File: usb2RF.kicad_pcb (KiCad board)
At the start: 4 copper layers, 40 x 15 mm, 38 parts, among them J1 USB_B_Micro, J2 SMA, J3 ARM 10Pin, U1 nRF24L01P, U2 XC6206P332MR, U3 USBLC6-2SC6, U4 STM32L432KBU6, Y1 16MHz

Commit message: [reLayout] [Router] Partially [FrontSilk]ZoomIn
Signed-off-by: EasonLiang <liangyx25@163.com>
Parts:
- C4, C7: footprint Capacitor_SMD:C_0402_1005Metric -> Capacitor_SMD:C_0603_1608Metric
- J1: footprint Connector_USB:USB_Micro-B_Molex-105017-0001 -> Connector_USB:USB_Mini-B_Lumberg_2486_01_Horizontal
- moved C18 2.36 mm to (48.9, 53.1)
- moved J3 1.91 mm to (55.7, 52.5)
- moved U3 1.89 mm to (52.6, 48.8)
- moved FB1 1.81 mm to (49.5, 41.4)
- moved C16 1.69 mm to (58.1, 51.2)
- moved C14 1.32 mm to (61.6, 42.8)
- moved J1 1.21 mm to (44.0, 49.1)
- moved C17 1.12 mm to (60.4, 42.7)
- moved C7 1.11 mm to (54.8, 44.6)
- moved U2 1.11 mm to (51.8, 44.9)
- moved U4 1.11 mm to (59.7, 47.5)
- moved C4 1.11 mm to (49.0, 45.1)
- moved C15 1.09 mm to (62.7, 42.8)
- moved R4 1.03 mm to (54.3, 40.9), turned to 180 degrees
- moved D1 0.96 mm to (56.9, 41.9)
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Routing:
- net GND: track 0.00 -> 40.5 mm
- net +3V3: track 0.00 -> 22.5 mm
- net +5V: track 0.00 -> 15.9 mm, vias 0 -> 2
- net SWCLK: track 0.00 -> 9.80 mm
- net SWDIO: track 0.00 -> 7.19 mm
- net Net-(C4-Pad1): track 0.00 -> 6.21 mm
- net NRF_XC1: track 0.00 -> 5.74 mm
- net USB_CONN_D+: track 0.00 -> 5.09 mm
- net USB_CONN_D-: track 0.00 -> 5.06 mm
- net NRF_IRQ: track 0.00 -> 4.64 mm
- net Net-(R3-Pad1): track 0.00 -> 3.87 mm
- net NRF_XC2: track 0.00 -> 3.81 mm
- net SPI3_ICS: track 0.00 -> 3.47 mm
- net NRF_CE: track 0.00 -> 3.47 mm
- net Net-(F1-Pad1): track 0.00 -> 3.29 mm
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
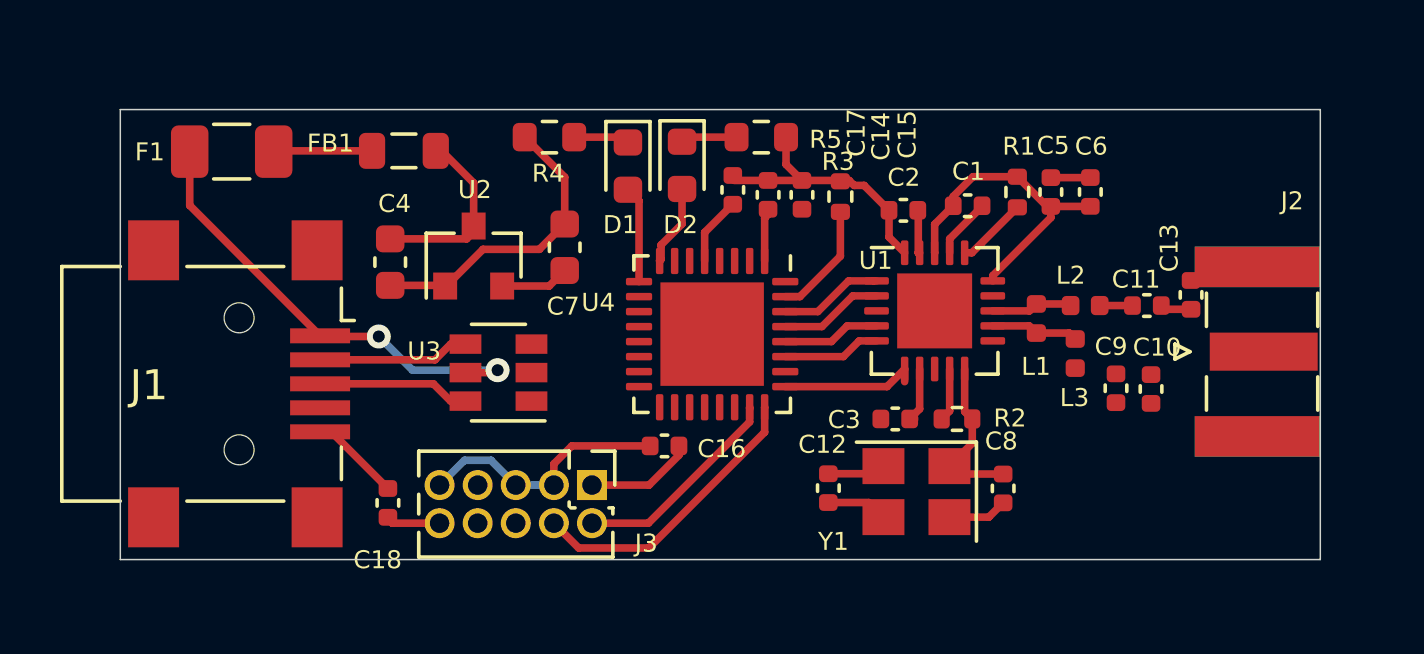
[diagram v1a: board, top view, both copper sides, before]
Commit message: [library List] both [PCB] update [schematic] update footprint
Signed-off-by: EasonLiang <liang_yongxin@apple.com>
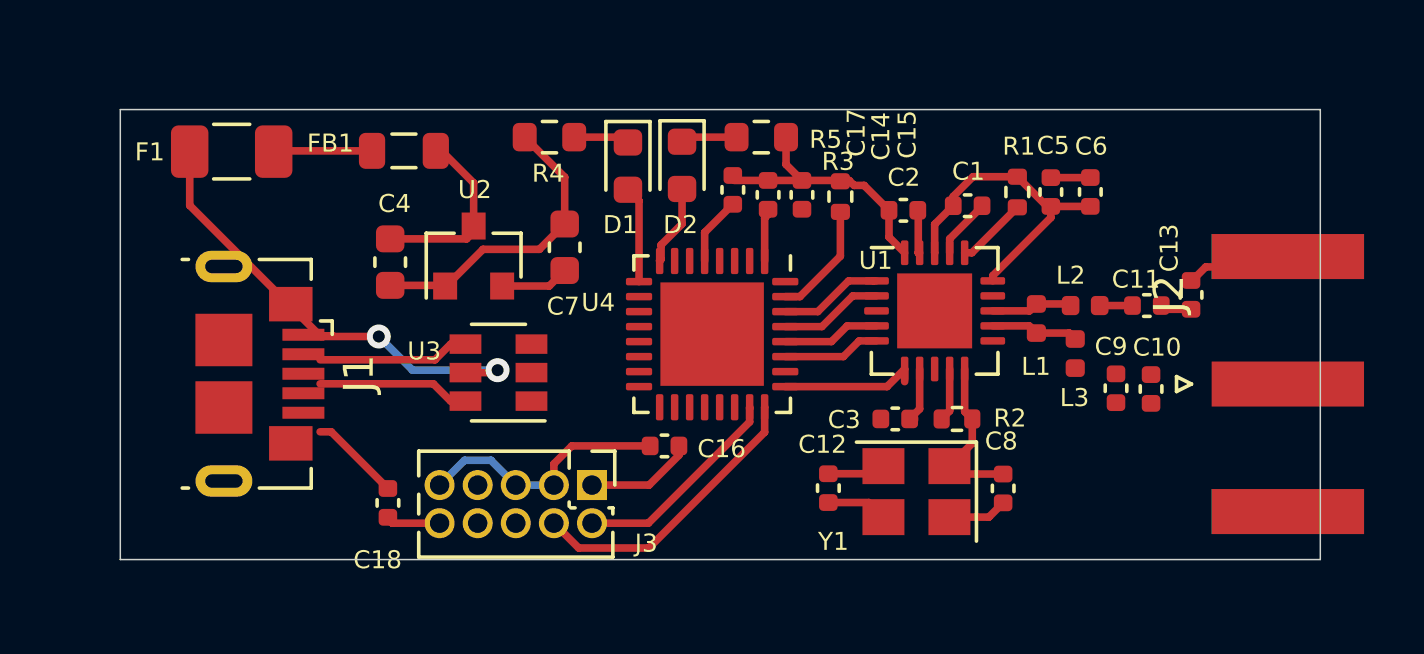
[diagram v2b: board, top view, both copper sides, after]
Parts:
- J1: footprint Connector_USB:USB_Mini-B_Lumberg_2486_01_Horizontal -> pcbEsLib:USB-Micro
- J2: footprint Connector_Coaxial:SMA_Samtec_SMA-J-P-X-ST-EM1_EdgeMount -> pcbEsLib:SMA_EdgeMount
- moved J2 1.47 mm to (78.9, 49.1), turned to 0 degrees
- moved J1 0.77 mm to (44.7, 48.8)
